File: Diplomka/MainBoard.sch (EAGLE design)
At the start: 29 parts, among them K1 ARK550/2, K2 ARK550/2, Q1 AP2012P3C-P22, Q2 BC817-40LT1SMD, SW1 TACTB-64K-F, SW2 TACTB-64K-F, SW3 TACTB-64K-F, U1 ESP32-WROOM-32, U2 AMS1117-3.3

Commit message: Schema v1.0 hotovo
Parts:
- removed SW1, SW2, SW3: TACTB-64K-F, #PaJa_prepinace:TACTB-64K-F
- added U$6, U$7, U$8: TS6604B, myParts:TS6604B
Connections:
- new net N$9: R10.1
- net BTN_OUTPUT: now also U$8.+; no longer SW3.1
- net GND: now also U$6.-, U$7.-, U$8.-; no longer SW1.1, SW2.2, SW3.2
- net N$7: now also U$6.+; no longer R10.1, SW1.2
- net N$8: now also U$7.+; no longer SW2.1
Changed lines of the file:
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@@
 <part name="R9" library="rcl" library_urn="urn:adsk.eagle:library:334" deviceset="R-EU_" device="R0805" package3d_urn="urn:adsk.eagle:package:23553/2" value="150"/>
 <part name="GND7" library="supply1" library_urn="urn:adsk.eagle:library:371" deviceset="GND" device=""/>
-<part name="SW1" library="#PaJa_prepinace" deviceset="TACTB-64K-F" device=""/>
 <part name="R10" library="rcl" library_urn="urn:adsk.eagle:library:334" deviceset="R-EU_" device="R0805" package3d_urn="urn:adsk.eagle:package:23553/2" value="10k"/>
 <part name="R11" library="rcl" library_urn="urn:adsk.eagle:library:334" deviceset="R-EU_" device="R0805" package3d_urn="urn:adsk.eagle:package:23553/2" value="10k"/>
-<part name="SW2" library="#PaJa_prepinace" deviceset="TACTB-64K-F" device=""/>
 <part name="R12" library="rcl" library_urn="urn:adsk.eagle:library:334" deviceset="R-EU_" device="R0805" package3d_urn="urn:adsk.eagle:package:23553/2" value="10k"/>
-<part name="SW3" library="#PaJa_prepinace" deviceset="TACTB-64K-F" device=""/>
 <part name="GND8" library="supply1" library_urn="urn:adsk.eagle:library:371" deviceset="GND" device=""/>
 <part name="U$5" library="myParts" deviceset="HTU21D" device=""/>
+<part name="U$6" library="myParts" deviceset="TS6604B" device=""/>
+<part name="U$7" library="myParts" deviceset="TS6604B" device=""/>
+<part name="U$8" library="myParts" deviceset="TS6604B" device=""/>
 </parts>
 <sheets>
@@
 <attribute name="VALUE" x="134.62" y="43.18" size="1.778" layer="96"/>
 </instance>
-<instance part="SW1" gate="TL" x="71.12" y="109.22" smashed="yes">
-<attribute name="NAME" x="71.755" y="111.125" size="1.778" layer="95"/>
-<attribute name="VALUE" x="76.2" y="107.95" size="1.778" layer="96" rot="R180"/>
-</instance>
 <instance part="R10" gate="G$1" x="78.74" y="116.84" smashed="yes" rot="R90">
 <attribute name="NAME" x="85.09" y="122.9614" size="1.778" layer="95" rot="R180"/>
@@
 <attribute name="VALUE" x="135.89" y="122.682" size="1.778" layer="96" rot="R180"/>
 </instance>
-<instance part="SW2" gate="TL" x="147.32" y="109.22" smashed="yes">
-<attribute name="NAME" x="147.955" y="111.125" size="1.778" layer="95"/>
-<attribute name="VALUE" x="152.4" y="107.95" size="1.778" layer="96" rot="R180"/>
-</instance>
 <instance part="R12" gate="G$1" x="104.14" y="27.94" smashed="yes" rot="R180">
 <attribute name="NAME" x="102.87" y="24.3586" size="1.778" layer="95"/>
 <attribute name="VALUE" x="102.87" y="22.098" size="1.778" layer="96"/>
 </instance>
-<instance part="SW3" gate="TL" x="124.46" y="27.94" smashed="yes">
-<attribute name="NAME" x="125.095" y="29.845" size="1.778" layer="95"/>
-<attribute name="VALUE" x="129.54" y="26.67" size="1.778" layer="96" rot="R180"/>
-</instance>
 <instance part="GND8" gate="1" x="137.16" y="25.4" smashed="yes">
 <attribute name="VALUE" x="134.62" y="22.86" size="1.778" layer="96"/>
 </instance>
+<instance part="U$6" gate="G$1" x="68.58" y="109.22" smashed="yes" rot="MR0"/>
+<instance part="U$7" gate="G$1" x="147.32" y="109.22" smashed="yes"/>
+<instance part="U$8" gate="G$1" x="127" y="27.94" smashed="yes"/>
 </instances>
 <busses>
@@
 </segment>
 <segment>
-<pinref part="SW1" gate="TL" pin="1"/>
-<wire x1="66.04" y1="109.22" x2="58.42" y2="109.22" width="0.1524" layer="91"/>
-<label x="58.42" y="109.22" size="1.778" layer="95" rot="R180" xref="yes"/>
-</segment>
-<segment>
-<pinref part="SW2" gate="TL" pin="2"/>
 <wire x1="152.4" y1="109.22" x2="154.94" y2="109.22" width="0.1524" layer="91"/>
 <label x="154.94" y="109.22" size="1.778" layer="95" xref="yes"/>
+<pinref part="U$7" gate="G$1" pin="-"/>
 </segment>
 <segment>
 <pinref part="GND8" gate="1" pin="GND"/>
-<pinref part="SW3" gate="TL" pin="2"/>
-<wire x1="137.16" y1="27.94" x2="129.54" y2="27.94" width="0.1524" layer="91"/>
+<wire x1="137.16" y1="27.94" x2="134.62" y2="27.94" width="0.1524" layer="91"/>
+<pinref part="U$8" gate="G$1" pin="-"/>
+<wire x1="134.62" y1="27.94" x2="129.54" y2="27.94" width="0.1524" layer="91"/>
+<junction x="134.62" y="27.94"/>
 </segment>
 <segment>
@@
 <junction x="213.36" y="63.5"/>
 </segment>
+<segment>
+<pinref part="U$6" gate="G$1" pin="-"/>
+<wire x1="60.96" y1="109.22" x2="53.34" y2="109.22" width="0.1524" layer="91"/>
+<label x="53.34" y="109.22" size="1.778" layer="95" rot="R180" xref="yes"/>
+</segment>
 </net>
 <net name="TXD0" class="0">
@@
 <net name="N$7" class="0">
 <segment>
-<pinref part="SW1" gate="TL" pin="2"/>
-<pinref part="R10" gate="G$1" pin="1"/>
-<wire x1="76.2" y1="109.22" x2="78.74" y2="109.22" width="0.1524" layer="91"/>
-<wire x1="78.74" y1="109.22" x2="78.74" y2="111.76" width="0.1524" layer="91"/>
 <pinref part="U1" gate="G$1" pin="EN"/>
-<wire x1="78.74" y1="109.22" x2="83.82" y2="109.22" width="0.1524" layer="91"/>
-<junction x="78.74" y="109.22"/>
+<wire x1="76.2" y1="109.22" x2="83.82" y2="109.22" width="0.1524" layer="91"/>
+<pinref part="U$6" gate="G$1" pin="+"/>
 </segment>
 </net>
@@
 <pinref part="U1" gate="G$1" pin="IO0"/>
 <wire x1="129.54" y1="109.22" x2="124.46" y2="109.22" width="0.1524" layer="91"/>
-<pinref part="SW2" gate="TL" pin="1"/>
-<wire x1="129.54" y1="109.22" x2="142.24" y2="109.22" width="0.1524" layer="91"/>
+<wire x1="129.54" y1="109.22" x2="139.7" y2="109.22" width="0.1524" layer="91"/>
 <junction x="129.54" y="109.22"/>
+<pinref part="U$7" gate="G$1" pin="+"/>
+<wire x1="139.7" y1="109.22" x2="142.24" y2="109.22" width="0.1524" layer="91"/>
+<junction x="139.7" y="109.22"/>
 </segment>
 </net>
 <net name="BTN_OUTPUT" class="0">
 <segment>
-<pinref part="SW3" gate="TL" pin="1"/>
 <pinref part="R12" gate="G$1" pin="1"/>
 <wire x1="119.38" y1="27.94" x2="114.3" y2="27.94" width="0.1524" layer="91"/>
@@
 <junction x="114.3" y="27.94"/>
 <label x="114.3" y="20.32" size="1.778" layer="95" xref="yes"/>
+<pinref part="U$8" gate="G$1" pin="+"/>
 </segment>
 <segment>
@@
 </segment>
 </net>
+<net name="N$9" class="0">
+<segment>
+<pinref part="R10" gate="G$1" pin="1"/>
+<wire x1="78.74" y1="109.22" x2="78.74" y2="111.76" width="0.1524" layer="91"/>
+</segment>
+</net>

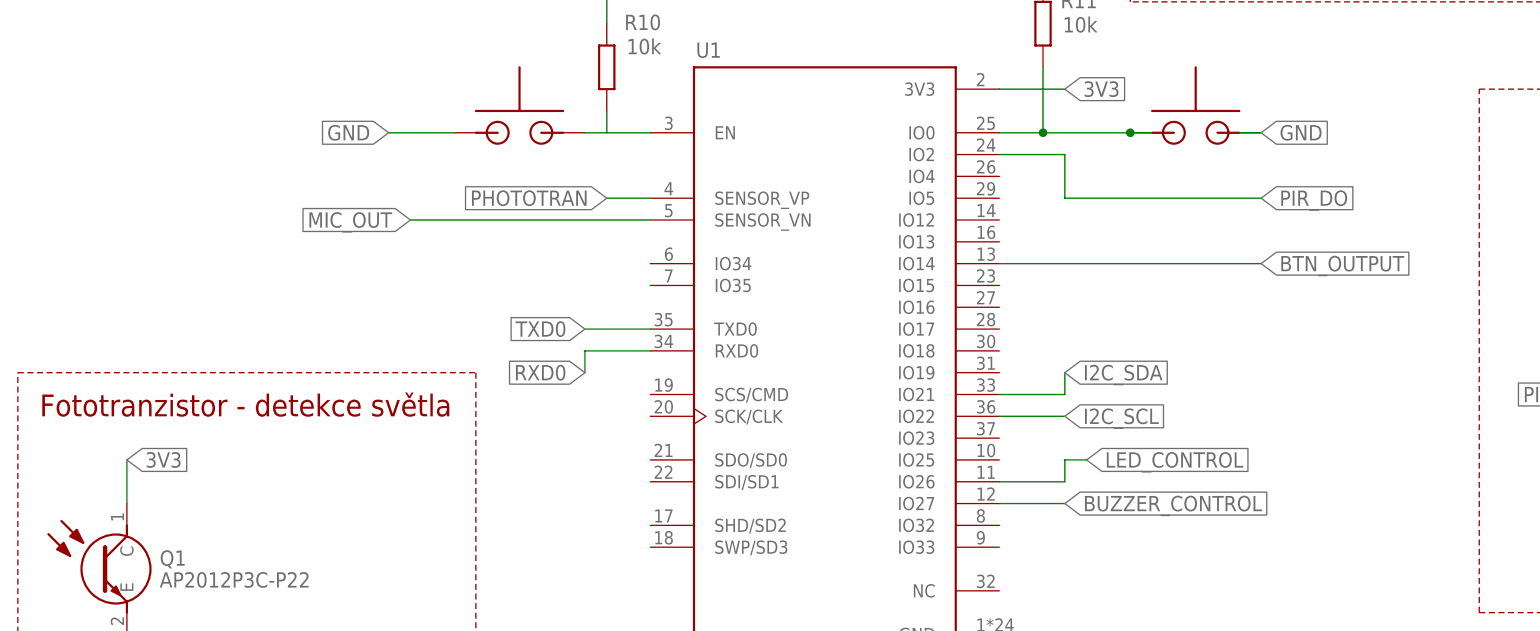
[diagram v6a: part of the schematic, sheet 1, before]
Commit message: Nektere soucastky nyni budou napajene z ESP32. Pridan soubor co obsahuje kosik v GME.
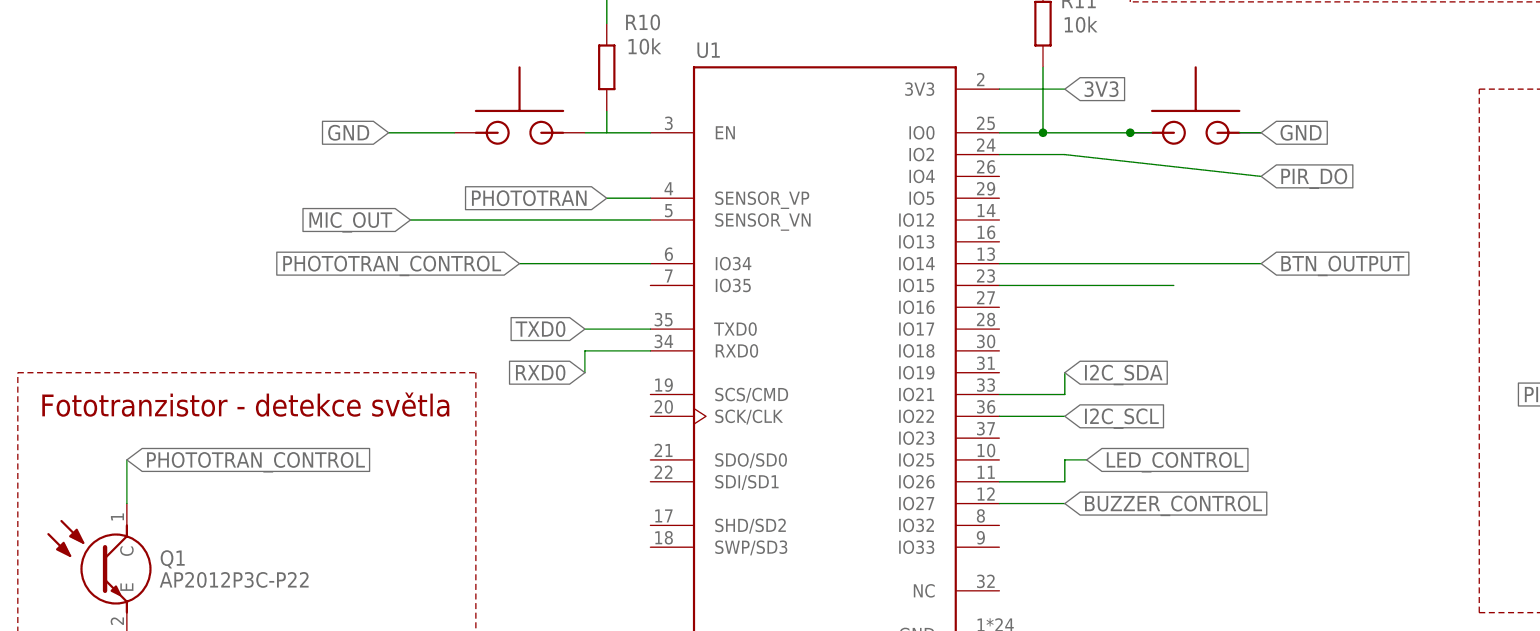
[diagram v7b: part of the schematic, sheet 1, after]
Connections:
- new net N$10: U1.IO15
- new net PHOTOTRAN_CONTROL: Q1.C, U1.IO34
- net 3V3: no longer Q1.C
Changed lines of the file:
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@@
-</segment>
-<segment>
-<pinref part="Q1" gate="G$1" pin="C"/>
-<wire x1="22.86" y1="66.04" x2="22.86" y2="71.12" width="0.1524" layer="91"/>
-<label x="22.86" y="71.12" size="1.778" layer="95" xref="yes"/>
 </segment>
 <segment>
@@
 <pinref part="U1" gate="G$1" pin="IO2"/>
 <wire x1="124.46" y1="106.68" x2="132.08" y2="106.68" width="0.1524" layer="91"/>
-<wire x1="132.08" y1="106.68" x2="132.08" y2="101.6" width="0.1524" layer="91"/>
-<wire x1="132.08" y1="101.6" x2="154.94" y2="101.6" width="0.1524" layer="91"/>
-<label x="154.94" y="101.6" size="1.778" layer="95" xref="yes"/>
+<wire x1="132.08" y1="106.68" x2="154.94" y2="104.14" width="0.1524" layer="91"/>
+<label x="154.94" y="104.14" size="1.778" layer="95" xref="yes"/>
 </segment>
 </net>
@@
 </segment>
 </net>
+<net name="N$10" class="0">
+<segment>
+<pinref part="U1" gate="G$1" pin="IO15"/>
+<wire x1="124.46" y1="91.44" x2="144.78" y2="91.44" width="0.1524" layer="91"/>
+</segment>
+</net>
+<net name="PHOTOTRAN_CONTROL" class="0">
+<segment>
+<pinref part="U1" gate="G$1" pin="IO34"/>
+<wire x1="83.82" y1="93.98" x2="68.58" y2="93.98" width="0.1524" layer="91"/>
+<label x="68.58" y="93.98" size="1.778" layer="95" rot="R180" xref="yes"/>
+</segment>
+<segment>
+<pinref part="Q1" gate="G$1" pin="C"/>
+<wire x1="22.86" y1="66.04" x2="22.86" y2="71.12" width="0.1524" layer="91"/>
+<label x="22.86" y="71.12" size="1.778" layer="95" xref="yes"/>
+</segment>
+</net>

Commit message: Zmeny v PCB
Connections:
- removed net N$10: U1.IO15
- new net MIC_CONTROL: U$3.OUT, U1.IO15
- new net TEMP_CONTROL: U$5.VIN, U1.IO17
- net 3V3: no longer U$5.VIN
- net MIC_OUT: no longer U$3.OUT
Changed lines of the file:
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@@
 <pinref part="U1" gate="G$1" pin="IO2"/>
 <wire x1="124.46" y1="106.68" x2="132.08" y2="106.68" width="0.1524" layer="91"/>
-<wire x1="132.08" y1="106.68" x2="154.94" y2="104.14" width="0.1524" layer="91"/>
 <label x="154.94" y="104.14" size="1.778" layer="95" xref="yes"/>
+<wire x1="154.94" y1="104.14" x2="132.08" y2="104.14" width="0.1524" layer="91"/>
+<wire x1="132.08" y1="104.14" x2="132.08" y2="106.68" width="0.1524" layer="91"/>
 </segment>
 </net>
@@
 <segment>
 <pinref part="U1" gate="G$1" pin="IO14"/>
-<wire x1="124.46" y1="93.98" x2="154.94" y2="93.98" width="0.1524" layer="91"/>
-<label x="154.94" y="93.98" size="1.778" layer="95" xref="yes"/>
+<wire x1="124.46" y1="93.98" x2="160.02" y2="93.98" width="0.1524" layer="91"/>
+<label x="160.02" y="93.98" size="1.778" layer="95" xref="yes"/>
 </segment>
 </net>
@@
 </segment>
 </net>
-<net name="N$10" class="0">
+<net name="MIC_CONTROL" class="0">
 <segment>
 <pinref part="U1" gate="G$1" pin="IO15"/>
-<wire x1="124.46" y1="91.44" x2="144.78" y2="91.44" width="0.1524" layer="91"/>
+<wire x1="124.46" y1="91.44" x2="132.08" y2="91.44" width="0.1524" layer="91"/>
+<label x="132.08" y="91.44" size="1.778" layer="95" xref="yes"/>
 </segment>
 </net>
@@
 <wire x1="22.86" y1="66.04" x2="22.86" y2="71.12" width="0.1524" layer="91"/>
 <label x="22.86" y="71.12" size="1.778" layer="95" xref="yes"/>
+</segment>
+</net>
+<net name="TEMP_CONTROL" class="0">
+<segment>
+<pinref part="U1" gate="G$1" pin="IO17"/>
+<wire x1="124.46" y1="86.36" x2="132.08" y2="86.36" width="0.1524" layer="91"/>
+<label x="132.08" y="86.36" size="1.778" layer="95" xref="yes"/>
 </segment>
 </net>
@@
 <label x="10.16" y="43.18" size="1.778" layer="95" rot="R180" xref="yes"/>
 </segment>
-<segment>
-<pinref part="U$5" gate="G$1" pin="VIN"/>
-<wire x1="43.18" y1="121.92" x2="38.1" y2="121.92" width="0.1524" layer="91"/>
-<label x="38.1" y="121.92" size="1.778" layer="95" rot="R180" xref="yes"/>
-</segment>
 </net>
 <net name="GND" class="0">
@@
 </segment>
 </net>
-<net name="MIC_OUT" class="0">
-<segment>
-<pinref part="U$3" gate="G$1" pin="OUT"/>
-<wire x1="25.4" y1="53.34" x2="10.16" y2="53.34" width="0.1524" layer="91"/>
-<label x="10.16" y="53.34" size="1.778" layer="95" rot="R180" xref="yes"/>
-</segment>
-</net>
 <net name="N$1" class="0">
 <segment>
@@
 </segment>
 </net>
+<net name="MIC_CONTROL" class="0">
+<segment>
+<pinref part="U$3" gate="G$1" pin="OUT"/>
+<wire x1="25.4" y1="53.34" x2="10.16" y2="53.34" width="0.1524" layer="91"/>
+<label x="10.16" y="53.34" size="1.778" layer="95" rot="R180" xref="yes"/>
+</segment>
+</net>
+<net name="TEMP_CONTROL" class="0">
+<segment>
+<pinref part="U$5" gate="G$1" pin="VIN"/>
+<wire x1="43.18" y1="121.92" x2="35.56" y2="121.92" width="0.1524" layer="91"/>
+<wire x1="35.56" y1="121.92" x2="35.56" y2="124.46" width="0.1524" layer="91"/>
+<label x="35.56" y="124.46" size="1.778" layer="95" rot="R180" xref="yes"/>
+</segment>
+</net>
